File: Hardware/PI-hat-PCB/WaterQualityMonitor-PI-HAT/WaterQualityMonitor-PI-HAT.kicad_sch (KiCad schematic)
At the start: 7 parts

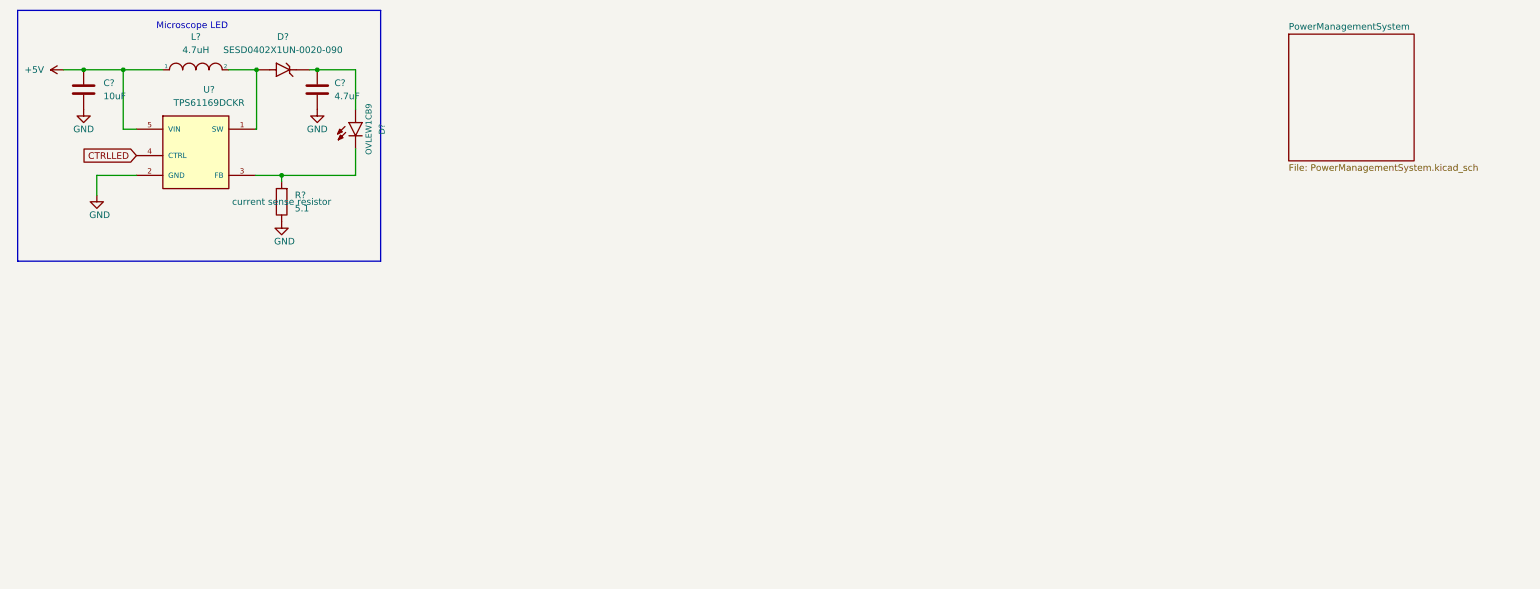
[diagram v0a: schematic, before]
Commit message: first attempt at stepper driver schematics
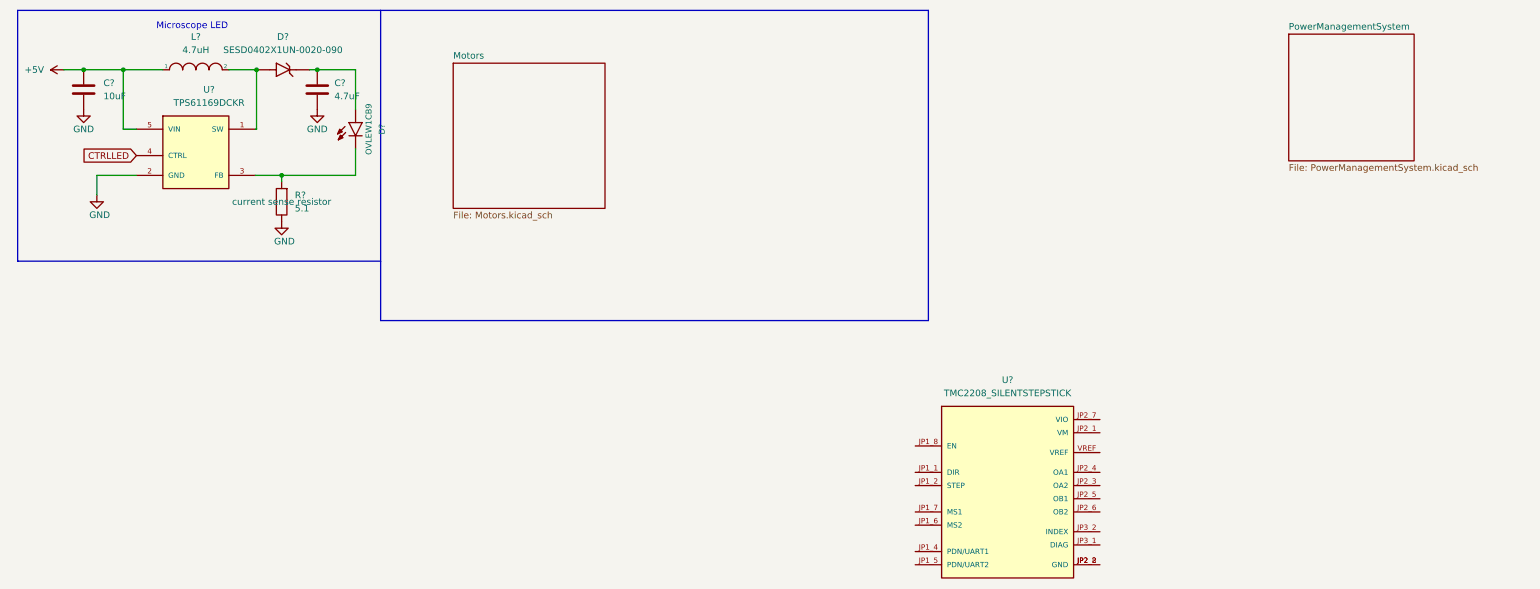
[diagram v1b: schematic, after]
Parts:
- added U?: TMC2208_SILENTSTEPSTICK, MODULE_TMC2208_SILENTSTEPSTICK, symbol TMC2208_SILENTSTEPSTICK:TMC2208_SILENTSTEPSTICK
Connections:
- new net: U?.JP2_2 (GND), U?.JP2_8 (GND)
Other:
- added sheet Motors (Motors.kicad_sch)
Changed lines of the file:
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@@
   (junction (at 25.4 24.13) (diameter 0) (color 0 0 0 0)
   )
+  (polyline (pts (xy 82.55 72.39) (xy 187.96 72.39))
+    (stroke (width 0) (type default) (color 0 0 0 0))
+  )
   (wire (pts (xy 63.5 44.45) (xy 63.5 45.72))
     (stroke (width 0) (type default) (color 0 0 0 0))
@@
     (stroke (width 0) (type default) (color 0 0 0 0))
   )
+  (polyline (pts (xy 82.55 60.96) (xy 82.55 72.39))
+    (stroke (width 0) (type default) (color 0 0 0 0))
+  )
+  (polyline (pts (xy 187.96 12.7) (xy 82.55 12.7))
+    (stroke (width 0) (type default) (color 0 0 0 0))
+  )
   (polyline (pts (xy 82.55 12.7) (xy 12.7 12.7))
     (stroke (width 0) (type default) (color 0 0 0 0))
@@
   )
   (wire (pts (xy 58.42 35.56) (xy 58.674 35.56))
+    (stroke (width 0) (type default) (color 0 0 0 0))
+  )
+  (polyline (pts (xy 187.96 72.39) (xy 187.96 12.7))
     (stroke (width 0) (type default) (color 0 0 0 0))
   )
@@
     (pin "2")
   )
+  (symbol (lib_id "TMC2208_SILENTSTEPSTICK:TMC2208_SILENTSTEPSTICK") (at 203.2 106.68 0) (unit 1)
+    (in_bom yes) (on_board yes) (fields_autoplaced)
+    (property "Reference" "U?" (id 0) (at 203.2 83.82 0))
+    (property "Value" "TMC2208_SILENTSTEPSTICK" (id 1) (at 203.2 86.36 0))
+    (property "Footprint" "MODULE_TMC2208_SILENTSTEPSTICK" (id 2) (at 187.96 125.73 0)
+      (effects (font (size 1.27 1.27)) (justify left bottom) hide)
+    )
+    (property "Datasheet" "" (id 3) (at 203.2 106.68 0)
+      (effects (font (size 1.27 1.27)) (justify left bottom) hide)
+    )
+    (property "MANUFACTURER" "Trinamic Motion" (id 4) (at 195.58 107.95 0)
+      (effects (font (size 1.27 1.27)) (justify left bottom) hide)
+    )
+    (pin "JP1_1")
+    (pin "JP1_2")
+    (pin "JP1_4")
+    (pin "JP1_5")
+    (pin "JP1_6")
+    (pin "JP1_7")
+    (pin "JP1_8")
+    (pin "JP2_1")
+    (pin "JP2_2")
+    (pin "JP2_3")
+    (pin "JP2_4")
+    (pin "JP2_5")
+    (pin "JP2_6")
+    (pin "JP2_7")
+    (pin "JP2_8")
+    (pin "JP3_1")
+    (pin "JP3_2")
+    (pin "VREF")
+  )
   (symbol (lib_id "Device:C") (at 70.358 27.94 0) (unit 1)
     (in_bom yes) (on_board yes) (fields_autoplaced)
@@
     )
     (pin "1")
+  )
+  (sheet (at 96.52 22.86) (size 29.21 27.94) (fields_autoplaced)
+    (stroke (width 0.1524) (type solid) (color 0 0 0 0))
+    (fill (color 0 0 0 0.0000))
+    (property "Sheet name" "Motors" (id 0) (at 96.52 22.1484 0)
+      (effects (font (size 1.27 1.27)) (justify left bottom))
+    )
+    (property "Sheet file" "Motors.kicad_sch" (id 1) (at 96.52 51.3846 0)
+      (effects (font (size 1.27 1.27)) (justify left top))
+    )
   )
   (sheet (at 257.302 17.272) (size 24.13 24.384) (fields_autoplaced)
@@
   (sheet_instances
     (path "/" (page "1"))
+    (path "/509754cd-dbf1-46e6-965c-38d41c0b6924" (page "3"))
     (path "/6c4087b1-d585-4615-84b3-d395a8b5856d" (page "3"))
   )
@@
       (reference "#PWR?") (unit 1) (value "GND") (footprint "")
     )
+    (path "/509754cd-dbf1-46e6-965c-38d41c0b6924/1cccede1-e9ff-4e29-9d8c-d30b3781567e"
+      (reference "#PWR?") (unit 1) (value "GND") (footprint "")
+    )
     (path "/6c4087b1-d585-4615-84b3-d395a8b5856d/25d8f479-e2c7-45aa-8859-43ba5028bb10"
       (reference "#PWR?") (unit 1) (value "GND") (footprint "")
@@
       (reference "#PWR?") (unit 1) (value "+3.3V") (footprint "")
     )
+    (path "/509754cd-dbf1-46e6-965c-38d41c0b6924/42302919-790e-4ef0-b556-2f6527ee333d"
+      (reference "#PWR?") (unit 1) (value "GND") (footprint "")
+    )
     (path "/6c4087b1-d585-4615-84b3-d395a8b5856d/42aa37c1-9c97-45ef-a3b0-f6f0a158dccb"
       (reference "#PWR?") (unit 1) (value "+5V") (footprint "")
     )
+    (path "/509754cd-dbf1-46e6-965c-38d41c0b6924/485978f9-2da4-4758-9a37-ea065688c12c"
+      (reference "#PWR?") (unit 1) (value "GND") (footprint "")
+    )
     (path "/6c4087b1-d585-4615-84b3-d395a8b5856d/4a157b4d-6b8c-4bf7-9e27-c08b4f0d478c"
+      (reference "#PWR?") (unit 1) (value "GND") (footprint "")
+    )
+    (path "/509754cd-dbf1-46e6-965c-38d41c0b6924/4a2684f3-8f0a-4fef-b91d-3e994c2016f1"
       (reference "#PWR?") (unit 1) (value "GND") (footprint "")
     )
@@
       (reference "R?") (unit 1) (value "5.1") (footprint "")
     )
+    (path "/509754cd-dbf1-46e6-965c-38d41c0b6924/07c85e68-0bf7-427d-95a2-4df276793fef"
+      (reference "U?") (unit 1) (value "TMC2208_SILENTSTEPSTICK") (footprint "MODULE_TMC2208_SILENTSTEPSTICK")
+    )
+    (path "/8af6c58a-1d90-4122-8f5b-13a5fb9fac6e"
+      (reference "U?") (unit 1) (value "TMC2208_SILENTSTEPSTICK") (footprint "MODULE_TMC2208_SILENTSTEPSTICK")
+    )
     (path "/bbc78703-4635-423a-a285-0138bfaaab5c"
       (reference "U?") (unit 1) (value "TPS61169DCKR") (footprint "SOT65P210X110-5N")
     )
-  )
+    (path "/509754cd-dbf1-46e6-965c-38d41c0b6924/c1dc1b77-ffa7-4f69-878e-c9530094aabf"
+      (reference "U?") (unit 1) (value "TMC2208_SILENTSTEPSTICK") (footprint "MODULE_TMC2208_SILENTSTEPSTICK")
+    )
+  )

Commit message: Finished Motor drivers and started PMS again
Now I actually removed the power management system
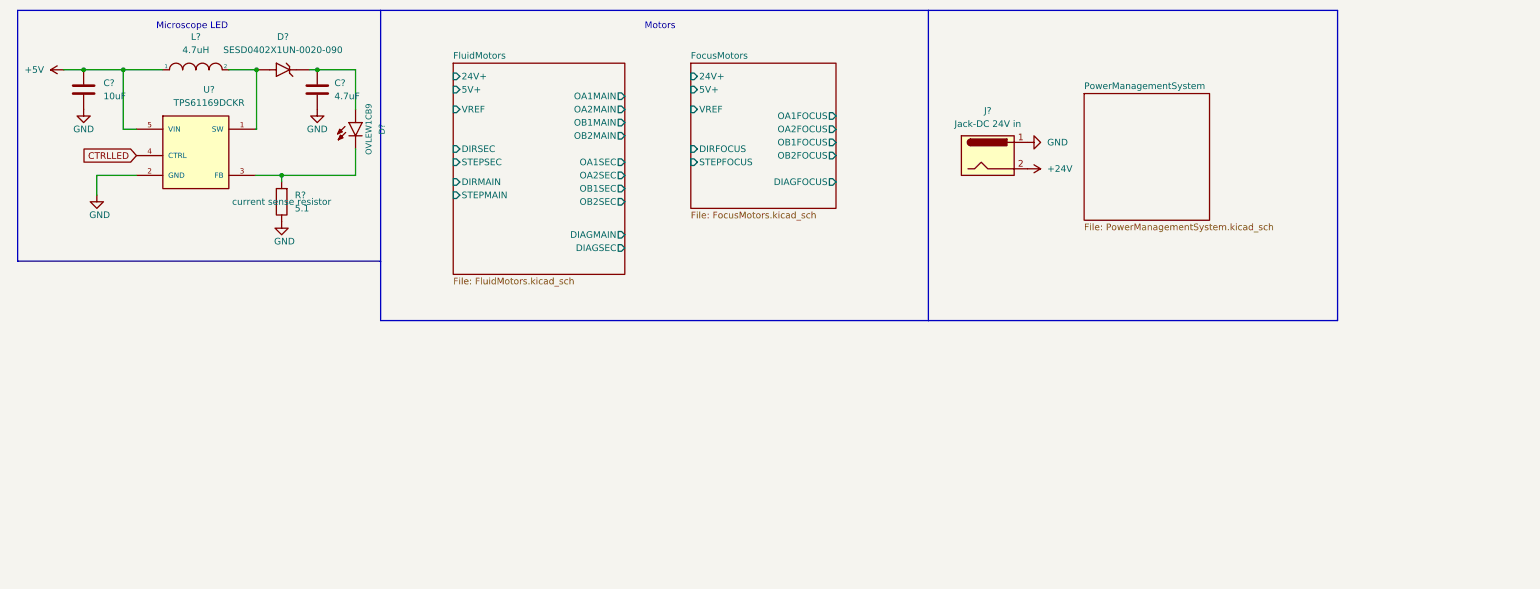
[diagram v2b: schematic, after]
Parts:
- removed U?: TMC2208_SILENTSTEPSTICK, MODULE_TMC2208_SILENTSTEPSTICK, symbol TMC2208_SILENTSTEPSTICK:TMC2208_SILENTSTEPSTICK
- added J?: Jack-DC 24V in, symbol Connector:Jack-DC
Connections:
- net GND: now also J?.1
- new net +24V: J?.2
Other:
- sheet Motors renamed FluidMotors
- added sheet FocusMotors (FocusMotors.kicad_sch)
- sheet FluidMotors: file Motors.kicad_sch -> FluidMotors.kicad_sch
- sheet FluidMotors ports: added 24V+, 5V+, DIAGMAIN, DIAGSEC, DIRMAIN, DIRSEC, OA1MAIN, OA1SEC, OA2MAIN, OA2SEC, OB1MAIN, OB1SEC, OB2MAIN, OB2SEC, STEPMAIN, STEPSEC, VREF; removed none
- note added: "Motors"

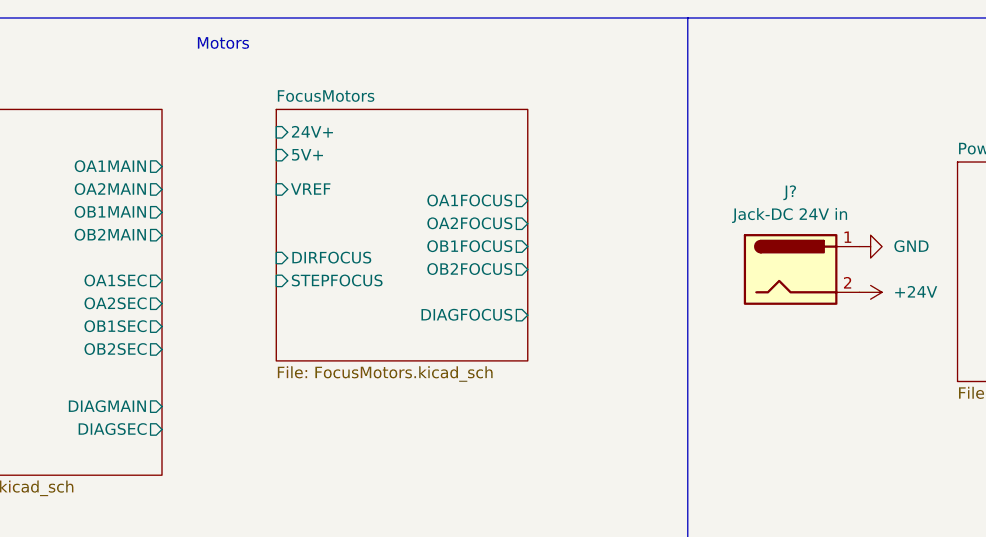
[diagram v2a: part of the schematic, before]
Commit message: placed components
First L should be checked, possibly not the right component
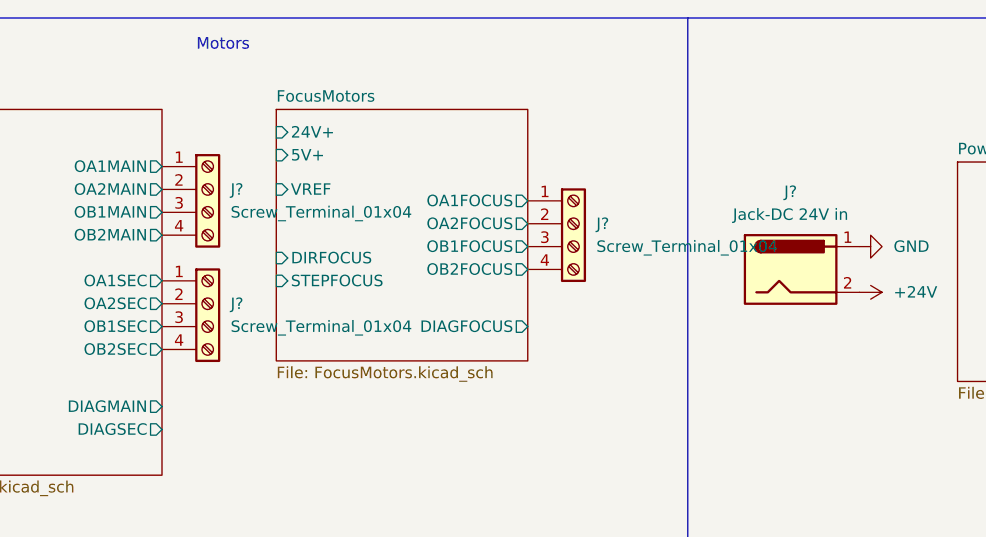
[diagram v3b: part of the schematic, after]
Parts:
- added J? (x3): Screw_Terminal_01x04, symbol Connector:Screw_Terminal_01x04
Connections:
- net FluidMotors/OA1MAIN: now also J?.1 (Pin_1)
- net FluidMotors/OA1SEC: now also J?.1 (Pin_1)
- net FluidMotors/OA2MAIN: now also J?.2 (Pin_2)
- net FluidMotors/OA2SEC: now also J?.2 (Pin_2)
- net FluidMotors/OB1MAIN: now also J?.3 (Pin_3)
- net FluidMotors/OB1SEC: now also J?.3 (Pin_3)
- net FluidMotors/OB2MAIN: now also J?.4 (Pin_4)
- net FluidMotors/OB2SEC: now also J?.4 (Pin_4)
- net FocusMotors/OA1FOCUS: now also J?.1 (Pin_1)
- net FocusMotors/OA2FOCUS: now also J?.2 (Pin_2)
- net FocusMotors/OB1FOCUS: now also J?.3 (Pin_3)
- net FocusMotors/OB2FOCUS: now also J?.4 (Pin_4)

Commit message: Finished powermanagementsystem
added RPI powersupply
added 5V and 3.3V power supply
changed some components (errors)
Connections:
- net +5V renamed 5V
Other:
- sheet PowerManagementSystem renamed RaspberryPiPower
- added sheet SensorsPower (SensorsPower.kicad_sch)
- sheet RaspberryPiPower: file PowerManagementSystem.kicad_sch -> RaspberryPiPower.kicad_sch
- sheet RaspberryPiPower ports: added 24V+, 5VRPI, GND; removed none
- note added: "PowerManagementSystem"
- moved on the sheet: J?

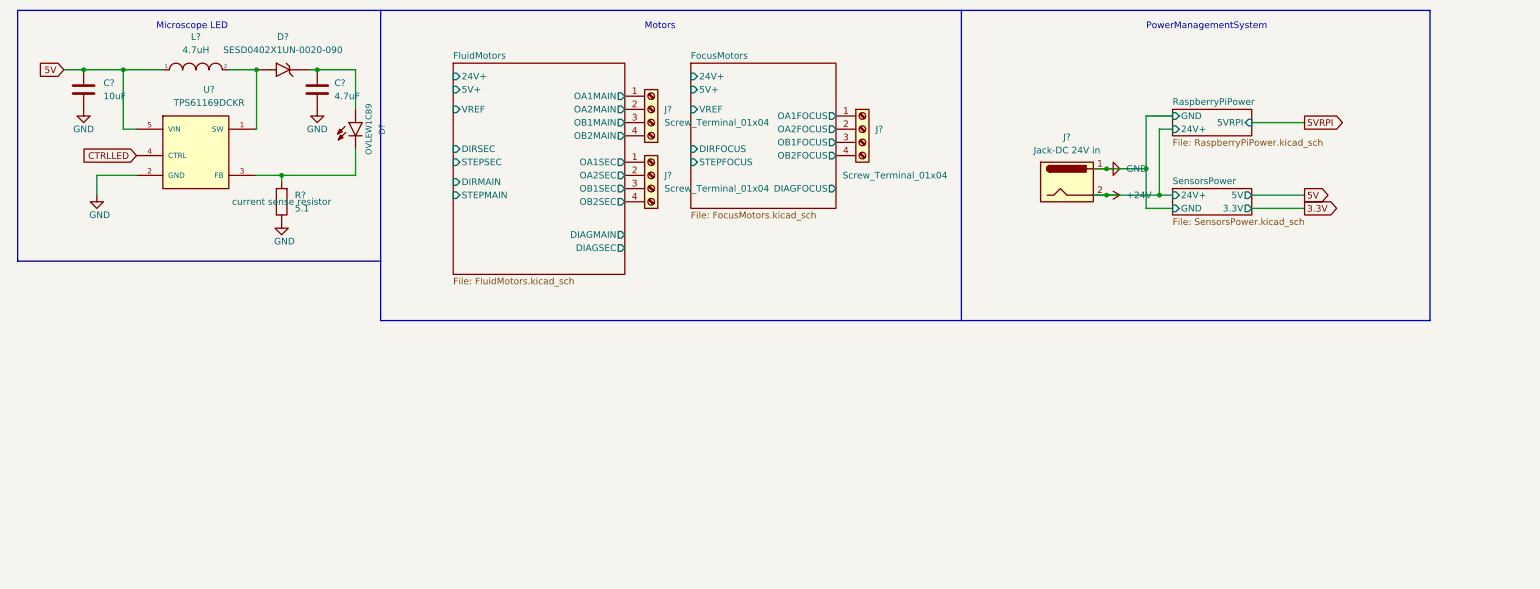
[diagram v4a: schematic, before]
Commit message: started heating and cooling design
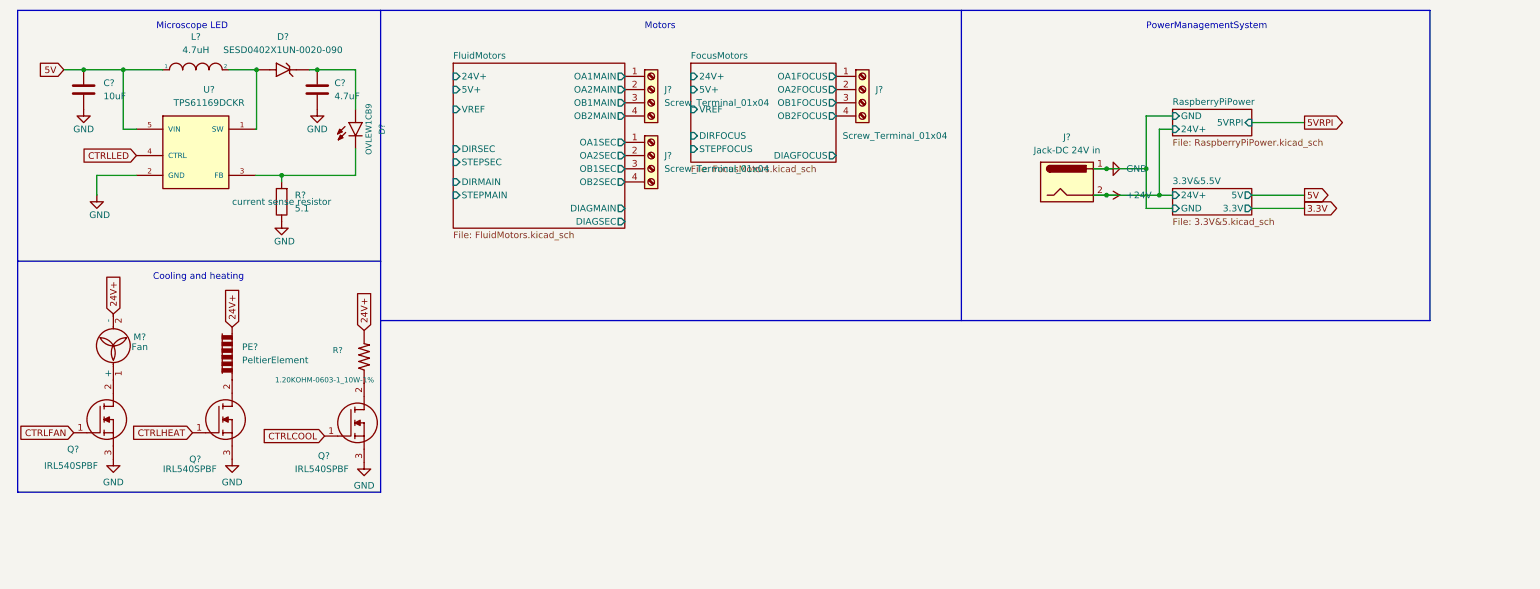
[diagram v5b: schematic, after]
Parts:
- added M?: Fan, symbol Motor:Fan
- added PE?: PeltierElement, symbol Device:PeltierElement
- added Q? (x3): IRL540SPBF, IRL540SPBF, symbol SamacSys_Parts:IRL540SPBF
- added R?: 1.20KOHM-0603-1_10W-1%, 0603, symbol SparkFun-Resistors:1.20KOHM-0603-1_10W-1%
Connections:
- net GND: now also Q?.3, Q?.3, Q?.3
- new net: PE?.1, Q?.2
- new net: M?.1 (+), Q?.2
- new net: Q?.2, R?.1
- new net 24V+: M?.2 (-), PE?.2, R?.2
- new net CTRLCOOL: Q?.1
- new net CTRLFAN: Q?.1
- new net CTRLHEAT: Q?.1
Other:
- sheet SensorsPower renamed 3.3V&5.5V
- sheet 3.3V&5.5V: file SensorsPower.kicad_sch -> 3.3V&5.kicad_sch
- note added: "Cooling and heating"
- moved on the sheet: J?

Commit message: Enhanced schematics
Moved protection circuits to main schematic
changed tmc2208 VIO to 3.3V (5V is also fine)
added fuses to heat and cooling schematic
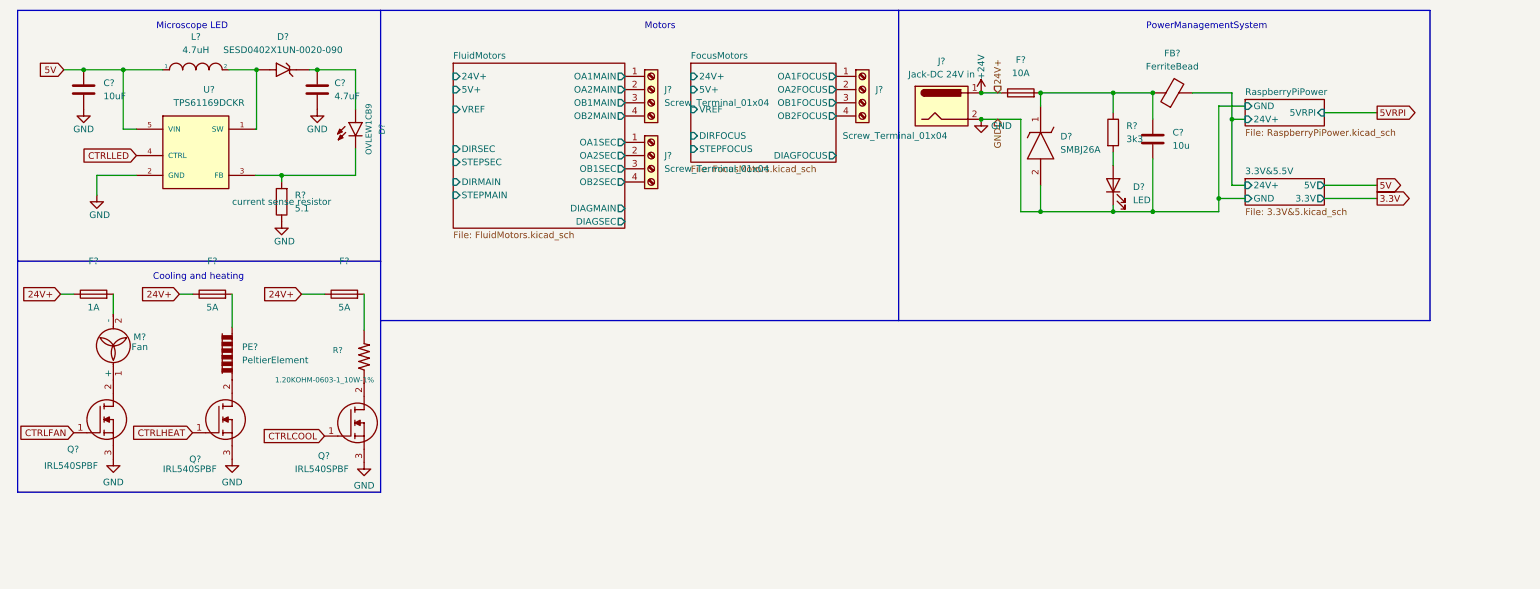
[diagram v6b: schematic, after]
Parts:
- added C?: 10u, symbol Device:C
- added D?: SMBJ26A, DIOM5436X244N, symbol SamacSys_Parts:SMBJ26A
- added D?: LED, symbol Device:LED
- added F? (x2): 5A, symbol Device:Fuse
- added F?: 10A, symbol Device:Fuse
- added F?: 1A, symbol Device:Fuse
- added FB?: FerriteBead, symbol Device:FerriteBead
- added R?: 3k3, symbol Device:R
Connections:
- net +24V: now also J?.1, F?.1, F?.1, F?.1, F?.1; no longer J?.2
- net GND: now also J?.2, C?.2, D?.1 (K), D?.2; no longer J?.1
- removed net 24V+: M?.2 (-), PE?.2, R?.2
- new net: F?.2, PE?.2
- new net: F?.2, M?.2 (-)
- new net: C?.1, D?.1, F?.2, FB?.1, R?.1
- new net: D?.2 (A), R?.2
- new net: F?.2, R?.2
- new net 3.3V&5.5V/24V+: FB?.2
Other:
- moved on the sheet: J?

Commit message: updated power management circuit
also added extra notes to  conversation 6.
added datasheet.
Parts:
- F?: value 1A -> 0.8A
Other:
- moved on the sheet: D?, F?, J?
